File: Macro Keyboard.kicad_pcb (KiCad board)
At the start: 2 copper layers, 101.6 x 123.4 mm, 135 parts, among them J2701 FPC 1x24, Q2701 Q_PJFET_GDS, SW1001 KH-PS1611-54, SW1101 KH-PS1611-54, SW1201 KH-PS1611-54, SW1301 KH-PS1611-54, SW1401 KH-PS1611-54, SW3001 SWITCH TACTILE SPST-NO 50MA 1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, SW501 KH-PS1611-54, SW601 KH-PS1611-54, SW701 KH-PS1611-54, SW801 KH-PS1611-54, SW901 KH-PS1611-54, U201 VEML7700, U2601 PCA9745BTWJ, U3001 Pico-JER, U301 PI4ULS5V201TAEX

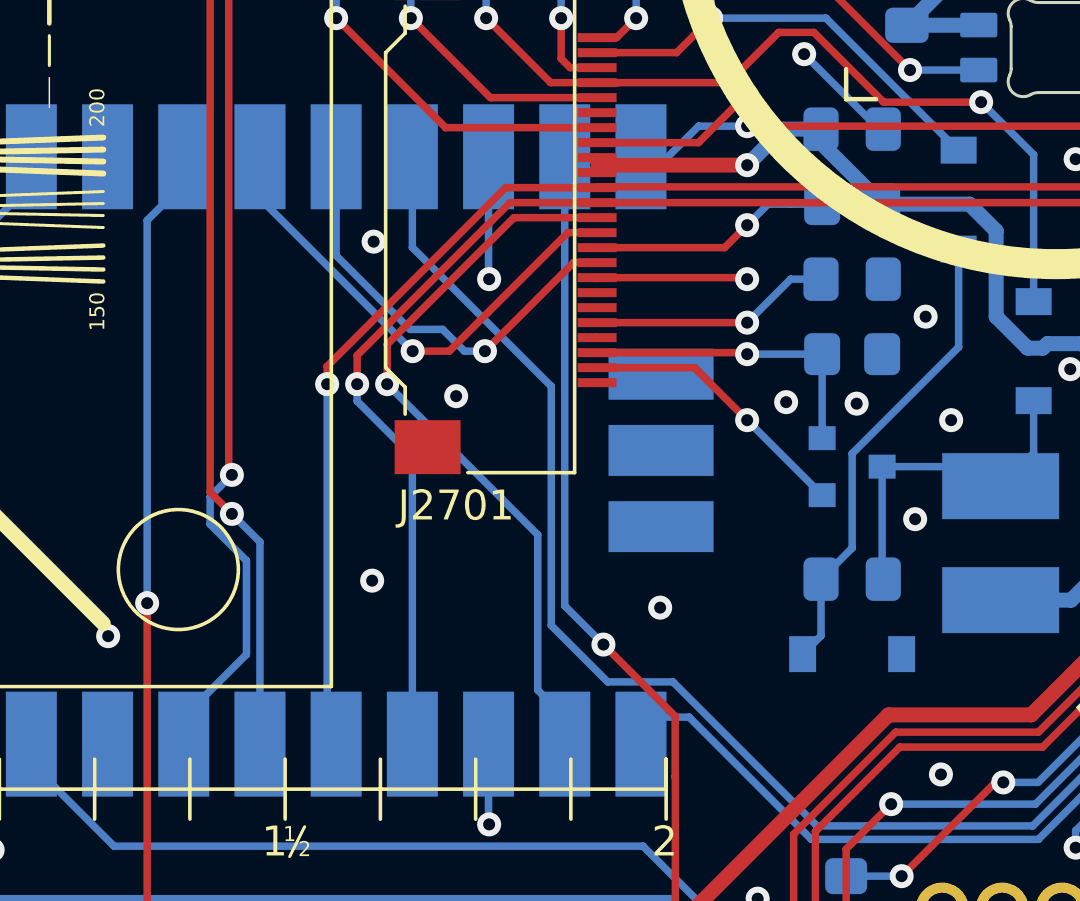
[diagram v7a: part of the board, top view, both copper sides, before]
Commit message: Updated so that eink reset pin is shared with GP04. Not ideal, but should work.
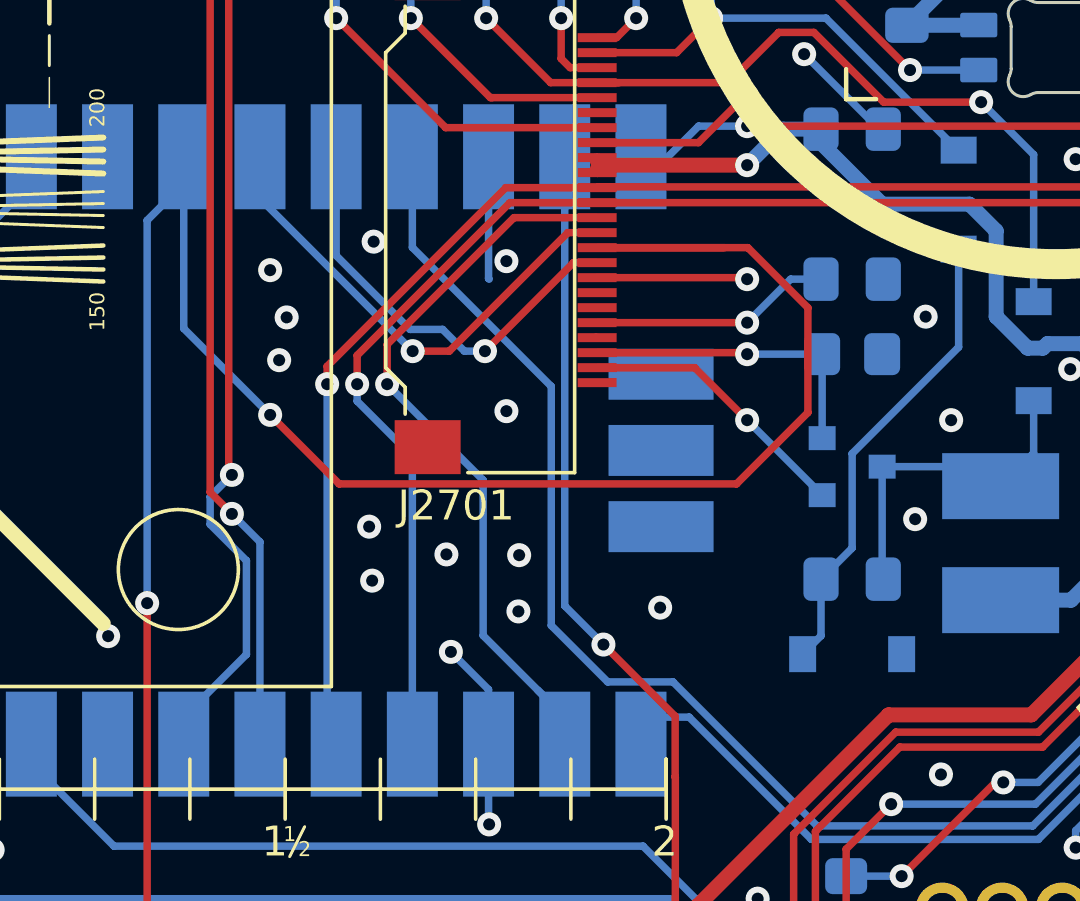
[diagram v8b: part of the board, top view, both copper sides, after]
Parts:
- removed R2702: 100k 5%, Resistor_SMD:R_0805_2012Metric_Pad1.20x1.40mm_HandSolder
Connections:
- J2701 pad 10: /eInk Display/DS_BS1 -> /SW4
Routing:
- net /SW4: track 36.1 -> 80.4 mm, vias 2 -> 3
- net /eInk Display/DS_BS1: track 8.10 -> 0.00 mm, vias 1 -> 0
- net GND: track 79.9 -> 82.6 mm, vias 113 -> 119
- net /DS_CS_3V3: track 24.3 -> 25.5 mm
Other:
- board text added: "P/N: 21-11.03-3 REV: A.R5 S/N:"
- board text removed: "P/N: 21-11.03-3 REV: A.R4 S/N:"
